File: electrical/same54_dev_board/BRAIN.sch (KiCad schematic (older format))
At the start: 8 parts, among them J2 Conn_ARM_JTAG_SWD_10, U1 p_ATSAME54P20A-AU, Y1 XOSC32, Y2 XOSC0

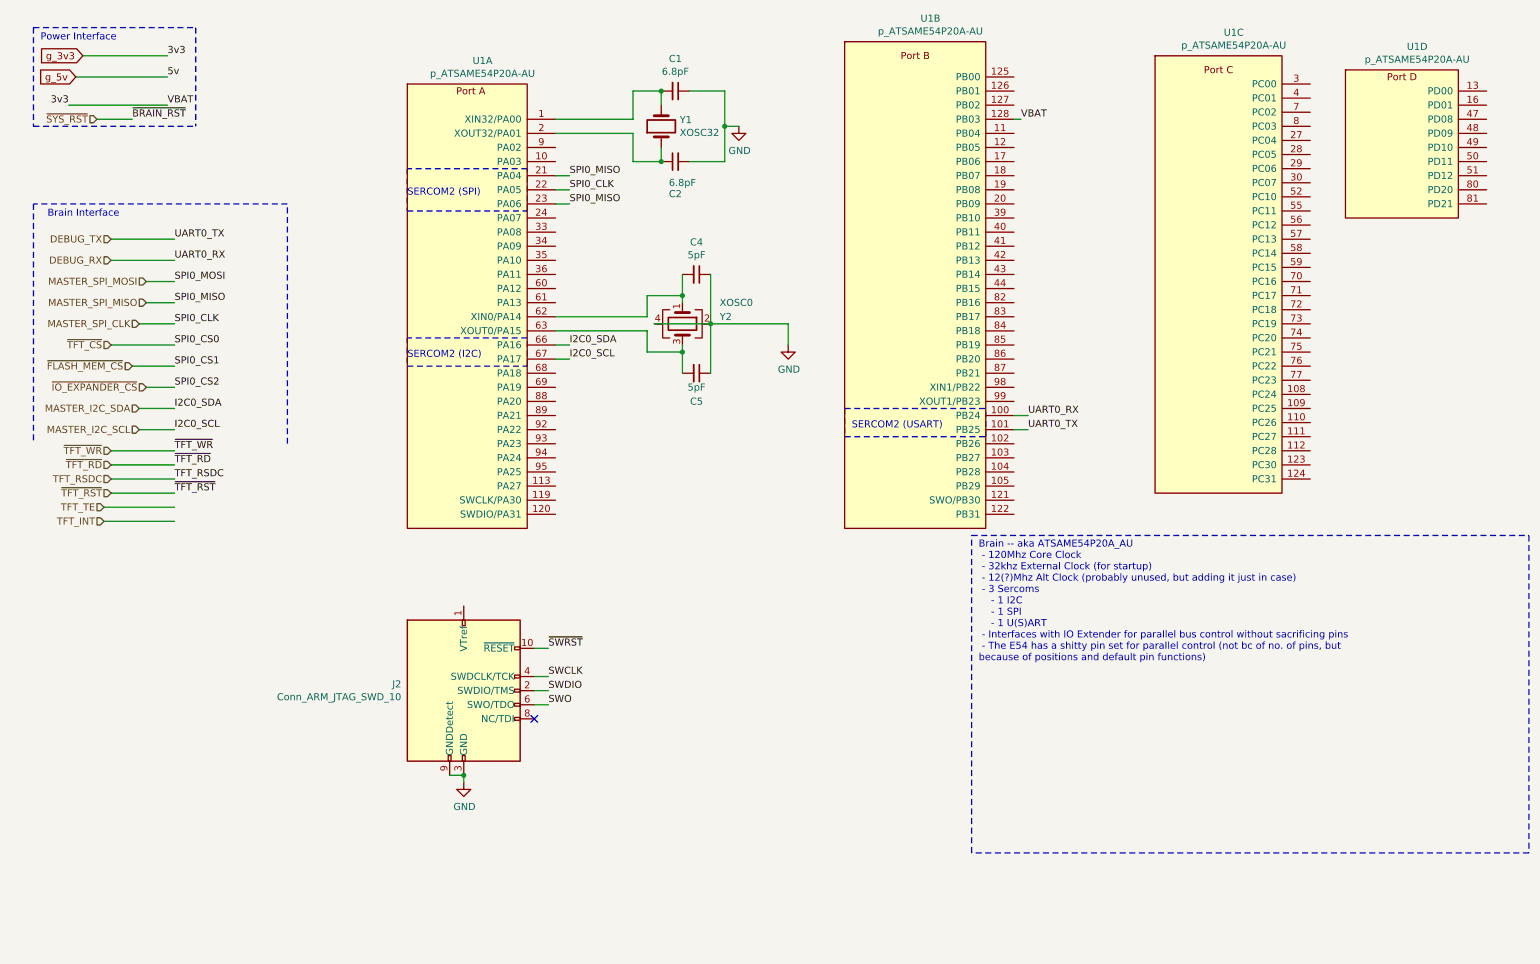
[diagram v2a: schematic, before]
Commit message: Made board smaller, changed some small things
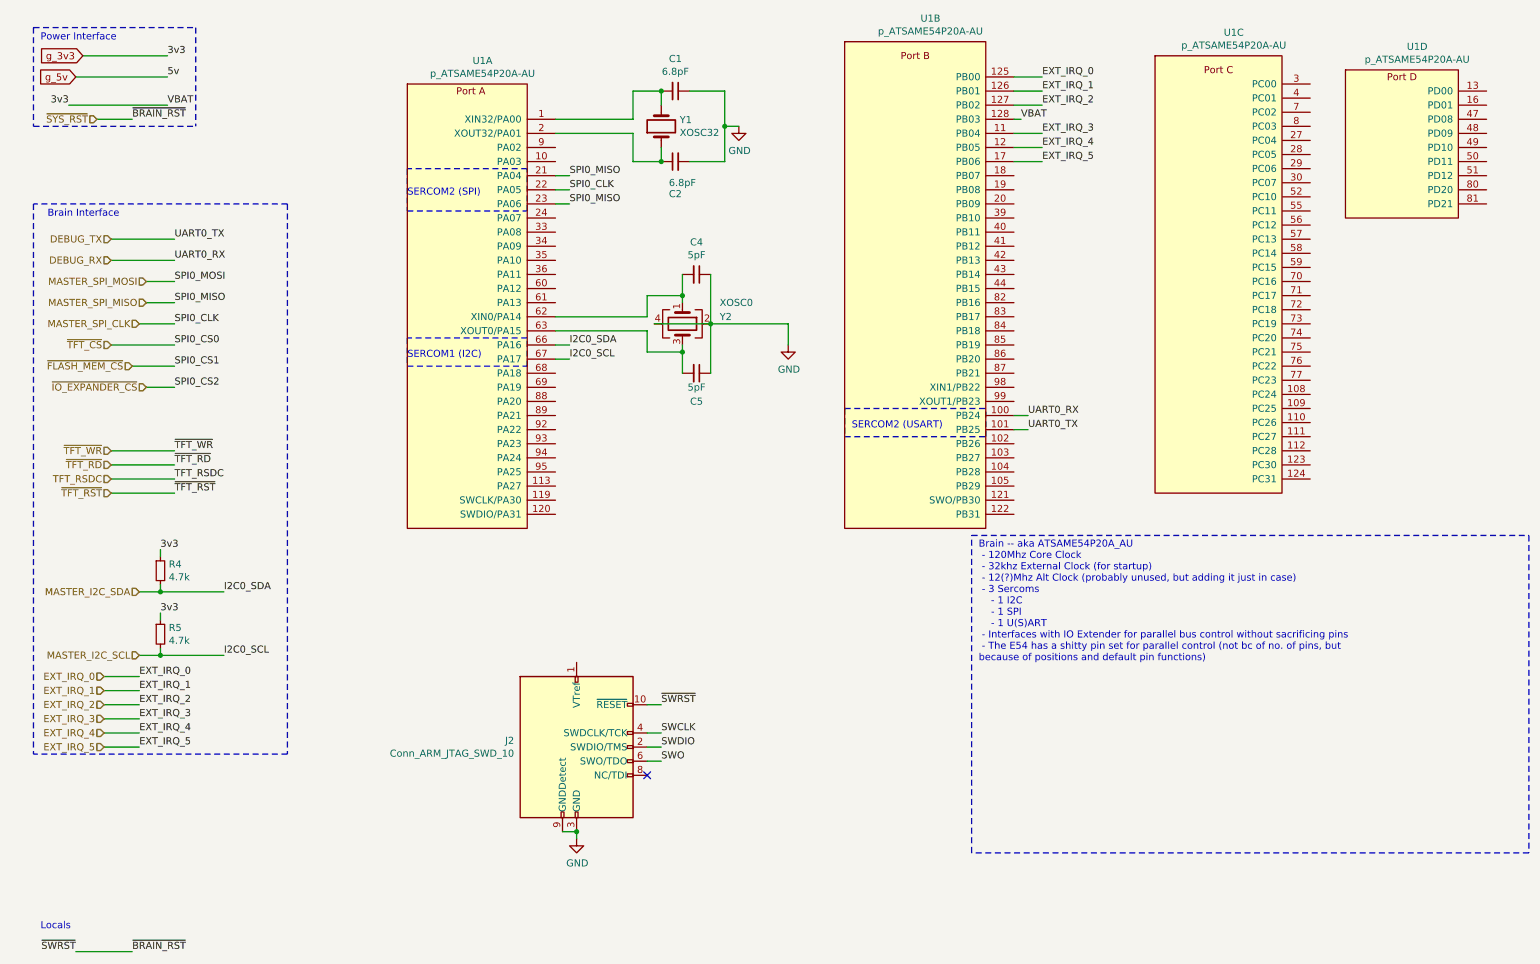
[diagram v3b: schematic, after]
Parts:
- added R4, R5: 4.7k, symbol Device:R_Small
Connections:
- net ~SWRST is gone; now on net ~SYS_RST: J2.10 (~RESET~)
- net MASTER_I2C_SCL: now also R5.2
- net MASTER_I2C_SDA: now also R4.2
- net g_3v3: now also R4.1, R5.1
- net EXT_IRQ_3: now reaches U1.11 (PB04)
- net EXT_IRQ_4: now reaches U1.12 (PB05)
- net EXT_IRQ_0: now reaches U1.125 (PB00)
- net EXT_IRQ_1: now reaches U1.126 (PB01)
- net EXT_IRQ_2: now reaches U1.127 (PB02)
- net EXT_IRQ_5: now reaches U1.17 (PB06)
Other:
- note added: "Locals"
- note added: "SERCOM1 (I2C)"
- note removed: "SERCOM2 (I2C)"
- moved on the sheet: J2
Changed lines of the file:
@@
 L Connector:Conn_ARM_JTAG_SWD_10 J2
 U 1 1 5EA1E350
-P 3600 5300
-F 0 "J2" H 3157 5346 50  0000 R CNN
-F 1 "Conn_ARM_JTAG_SWD_10" H 3157 5255 50  0000 R CNN
-F 2 "Connector_PinHeader_1.27mm:PinHeader_2x05_P1.27mm_Vertical" H 3600 5300 50  0001 C CNN
-F 3 "http://infocenter.arm.com/help/topic/com.arm.doc.ddi0314h/DDI0314H_coresight_components_trm.pdf" V 3250 4050 50  0001 C CNN
-	1    3600 5300
+P 4400 5700
+F 0 "J2" H 3957 5746 50  0000 R CNN
+F 1 "Conn_ARM_JTAG_SWD_10" H 3957 5655 50  0000 R CNN
+F 2 "Connector_PinHeader_1.27mm:PinHeader_2x05_P1.27mm_Vertical" H 4400 5700 50  0001 C CNN
+F 3 "http://infocenter.arm.com/help/topic/com.arm.doc.ddi0314h/DDI0314H_coresight_components_trm.pdf" V 4050 4450 50  0001 C CNN
+	1    4400 5700
 	1    0    0    -1
 $EndComp
@@
 Text HLabel 1250 3000 0    50   Input ~ 0
 ~FLASH_MEM_CS
-Text HLabel 1300 3300 0    50   Input ~ 0
-MASTER_I2C_SDA
-Text HLabel 1300 3450 0    50   Input ~ 0
-MASTER_I2C_SCL
 Wire Wire Line
 	1350 2400 1550 2400
@@
 Wire Wire Line
 	1250 3000 1550 3000
-Wire Wire Line
-	1300 3300 1550 3300
-Wire Wire Line
-	1300 3450 1550 3450
 Text HLabel 1350 3150 0    50   Input ~ 0
 ~IO_EXPANDER_CS
@@
 Text Notes 650  1950 0    50   ~ 0
 Brain Interface
-Wire Notes Line
-	550  1850 550  3550
-Wire Notes Line
-	2350 3550 2350 1850
 Wire Notes Line
 	2350 1850 550  1850
@@
 Text Label 1550 3150 0    50   ~ 0
 SPI0_CS2
-Text Label 1550 3300 0    50   ~ 0
-I2C0_SDA
-Text Label 1550 3450 0    50   ~ 0
-I2C0_SCL
 Text Label 7550 1250 0    50   ~ 0
 VBAT
@@
 Wire Wire Line
 	1100 3800 1550 3800
-Text Label 1550 3600 0    50   ~ 0
-~TFT_WR
 Text Label 1550 3700 0    50   ~ 0
 ~TFT_RD
@@
 Text Label 1550 3900 0    50   ~ 0
 ~TFT_RST
-Text HLabel 1050 4000 0    50   Input ~ 0
-TFT_TE
-Text HLabel 1050 4100 0    50   Input ~ 0
-TFT_INT
-Wire Wire Line
-	1050 4100 1550 4100
-Wire Wire Line
-	1050 4000 1550 4000
 Wire Wire Line
 	4250 1850 4350 1850
@@
 I2C0_SCL
 Text Notes 3200 2950 0    50   ~ 0
-SERCOM2 (I2C)
+SERCOM1 (I2C)
 Wire Notes Line
 	4050 2800 3200 2800
@@
 	4050 3000 4050 2800
 Wire Wire Line
-	4100 5000 4200 5000
+	4900 5400 5000 5400
 Text HLabel 1000 1250 0    50   Input ~ 0
 ~SYS_RST
@@
 	1000 1250 1250 1250
 Wire Wire Line
-	4100 5200 4200 5200
-Text Label 4200 5200 0    50   ~ 0
+	4900 5600 5000 5600
+Text Label 5000 5600 0    50   ~ 0
 SWCLK
 Wire Wire Line
-	4100 5300 4200 5300
-Text Label 4200 5300 0    50   ~ 0
+	4900 5700 5000 5700
+Text Label 5000 5700 0    50   ~ 0
 SWDIO
-Text Label 4200 5400 0    50   ~ 0
+Text Label 5000 5800 0    50   ~ 0
 SWO
 Wire Wire Line
-	4100 5400 4200 5400
-Wire Wire Line
-	3500 5900 3600 5900
-NoConn ~ 4100 5500
-Text Label 4200 5000 0    50   ~ 0
+	4900 5800 5000 5800
+Wire Wire Line
+	4300 6300 4400 6300
+NoConn ~ 4900 5900
+Text Label 5000 5400 0    50   ~ 0
 ~SWRST
 Wire Wire Line
-	3600 5900 3600 5950
-Connection ~ 3600 5900
-$Comp
-L power:GND #PWR?
+	4400 6300 4400 6350
+Connection ~ 4400 6300
+$Comp
+L power:GND #PWR0119
 U 1 1 5EA9AF4B
-P 3600 5950
-F 0 "#PWR?" H 3600 5700 50  0001 C CNN
-F 1 "GND" H 3605 5777 50  0000 C CNN
-F 2 "" H 3600 5950 50  0001 C CNN
-F 3 "" H 3600 5950 50  0001 C CNN
-	1    3600 5950
-	1    0    0    -1
-$EndComp
+P 4400 6350
+F 0 "#PWR0119" H 4400 6100 50  0001 C CNN
+F 1 "GND" H 4405 6177 50  0000 C CNN
+F 2 "" H 4400 6350 50  0001 C CNN
+F 3 "" H 4400 6350 50  0001 C CNN
+	1    4400 6350
+	1    0    0    -1
+$EndComp
+Text Label 1550 3600 0    50   ~ 0
+~TFT_WR
+Text Label 1900 5050 0    50   ~ 0
+I2C0_SCL
+Text Label 1900 4600 0    50   ~ 0
+I2C0_SDA
+Text HLabel 1300 5050 0    50   Input ~ 0
+MASTER_I2C_SCL
+Text HLabel 1300 4600 0    50   Input ~ 0
+MASTER_I2C_SDA
+$Comp
+L Device:R_Small R4
+U 1 1 5EB11658
+P 1450 4450
+F 0 "R4" H 1509 4496 50  0000 L CNN
+F 1 "4.7k" H 1509 4405 50  0000 L CNN
+F 2 "" H 1450 4450 50  0001 C CNN
+F 3 "~" H 1450 4450 50  0001 C CNN
+	1    1450 4450
+	1    0    0    -1
+$EndComp
+Wire Wire Line
+	1450 4350 1450 4300
+Text Label 1450 4300 0    50   ~ 0
+3v3
+$Comp
+L Device:R_Small R5
+U 1 1 5EB38D15
+P 1450 4900
+F 0 "R5" H 1509 4946 50  0000 L CNN
+F 1 "4.7k" H 1509 4855 50  0000 L CNN
+F 2 "" H 1450 4900 50  0001 C CNN
+F 3 "~" H 1450 4900 50  0001 C CNN
+	1    1450 4900
+	1    0    0    -1
+$EndComp
+Wire Wire Line
+	1300 5050 1450 5050
+Wire Wire Line
+	1300 4600 1450 4600
+Wire Wire Line
+	1450 4600 1450 4550
+Connection ~ 1450 4600
+Wire Wire Line
+	1450 4600 1900 4600
+Wire Wire Line
+	1450 5050 1450 5000
+Connection ~ 1450 5050
+Wire Wire Line
+	1450 4800 1450 4750
+Text Label 1450 4750 0    50   ~ 0
+3v3
+Wire Wire Line
+	1450 5050 1900 5050
+Text Label 850  7150 2    50   ~ 0
+~SWRST
+Wire Wire Line
+	850  7150 1250 7150
+Text Label 1250 7150 0    50   ~ 0
+~BRAIN_RST
+Text Notes 600  7000 0    50   ~ 0
+Locals
+Text HLabel 1050 5200 0    50   Input ~ 0
+EXT_IRQ_0
+Text HLabel 1050 5300 0    50   Input ~ 0
+EXT_IRQ_1
+Text HLabel 1050 5400 0    50   Input ~ 0
+EXT_IRQ_2
+Text HLabel 1050 5500 0    50   Input ~ 0
+EXT_IRQ_3
+Text HLabel 1050 5600 0    50   Input ~ 0
+EXT_IRQ_4
+Text HLabel 1050 5700 0    50   Input ~ 0
+EXT_IRQ_5
+Wire Wire Line
+	1050 5200 1300 5200
+Text Label 1300 5200 0    50   ~ 0
+EXT_IRQ_0
+Wire Wire Line
+	1050 5300 1300 5300
+Text Label 1300 5300 0    50   ~ 0
+EXT_IRQ_1
+Wire Wire Line
+	1050 5400 1300 5400
+Text Label 1300 5400 0    50   ~ 0
+EXT_IRQ_2
+Wire Wire Line
+	1050 5500 1300 5500
+Text Label 1300 5500 0    50   ~ 0
+EXT_IRQ_3
+Wire Wire Line
+	1050 5600 1300 5600
+Text Label 1300 5600 0    50   ~ 0
+EXT_IRQ_4
+Wire Wire Line
+	1050 5700 1300 5700
+Text Label 1300 5700 0    50   ~ 0
+EXT_IRQ_5
+Text Label 7700 950  0    50   ~ 0
+EXT_IRQ_0
+Wire Wire Line
+	7500 950  7700 950
+Text Label 7700 1050 0    50   ~ 0
+EXT_IRQ_1
+Wire Wire Line
+	7500 1050 7700 1050
+Text Label 7700 1150 0    50   ~ 0
+EXT_IRQ_2
+Wire Wire Line
+	7500 1150 7700 1150
+Wire Wire Line
+	7500 1450 7700 1450
+Text Label 7700 1450 0    50   ~ 0
+EXT_IRQ_4
+Wire Wire Line
+	7500 1350 7700 1350
+Text Label 7700 1350 0    50   ~ 0
+EXT_IRQ_3
+Wire Wire Line
+	7500 1550 7700 1550
+Text Label 7700 1550 0    50   ~ 0
+EXT_IRQ_5
+Wire Notes Line
+	2350 5750 550  5750
+Wire Notes Line
+	550  1850 550  5750
+Wire Notes Line
+	2350 1850 2350 5750
 $EndSCHEMATC

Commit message: migrating to laptop
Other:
- note added: "SERCOM0 (SPI)"
- note removed: "SERCOM2 (SPI)"
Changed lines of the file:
@@
 	4050 1900 4050 1600
 Text Notes 3200 1800 0    50   ~ 0
-SERCOM2 (SPI)
+SERCOM0 (SPI)
 Wire Wire Line
 	4250 2850 4350 2850
